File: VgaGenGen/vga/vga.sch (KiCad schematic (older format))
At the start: 26 parts, among them X25.175MHz CXO_DIP14

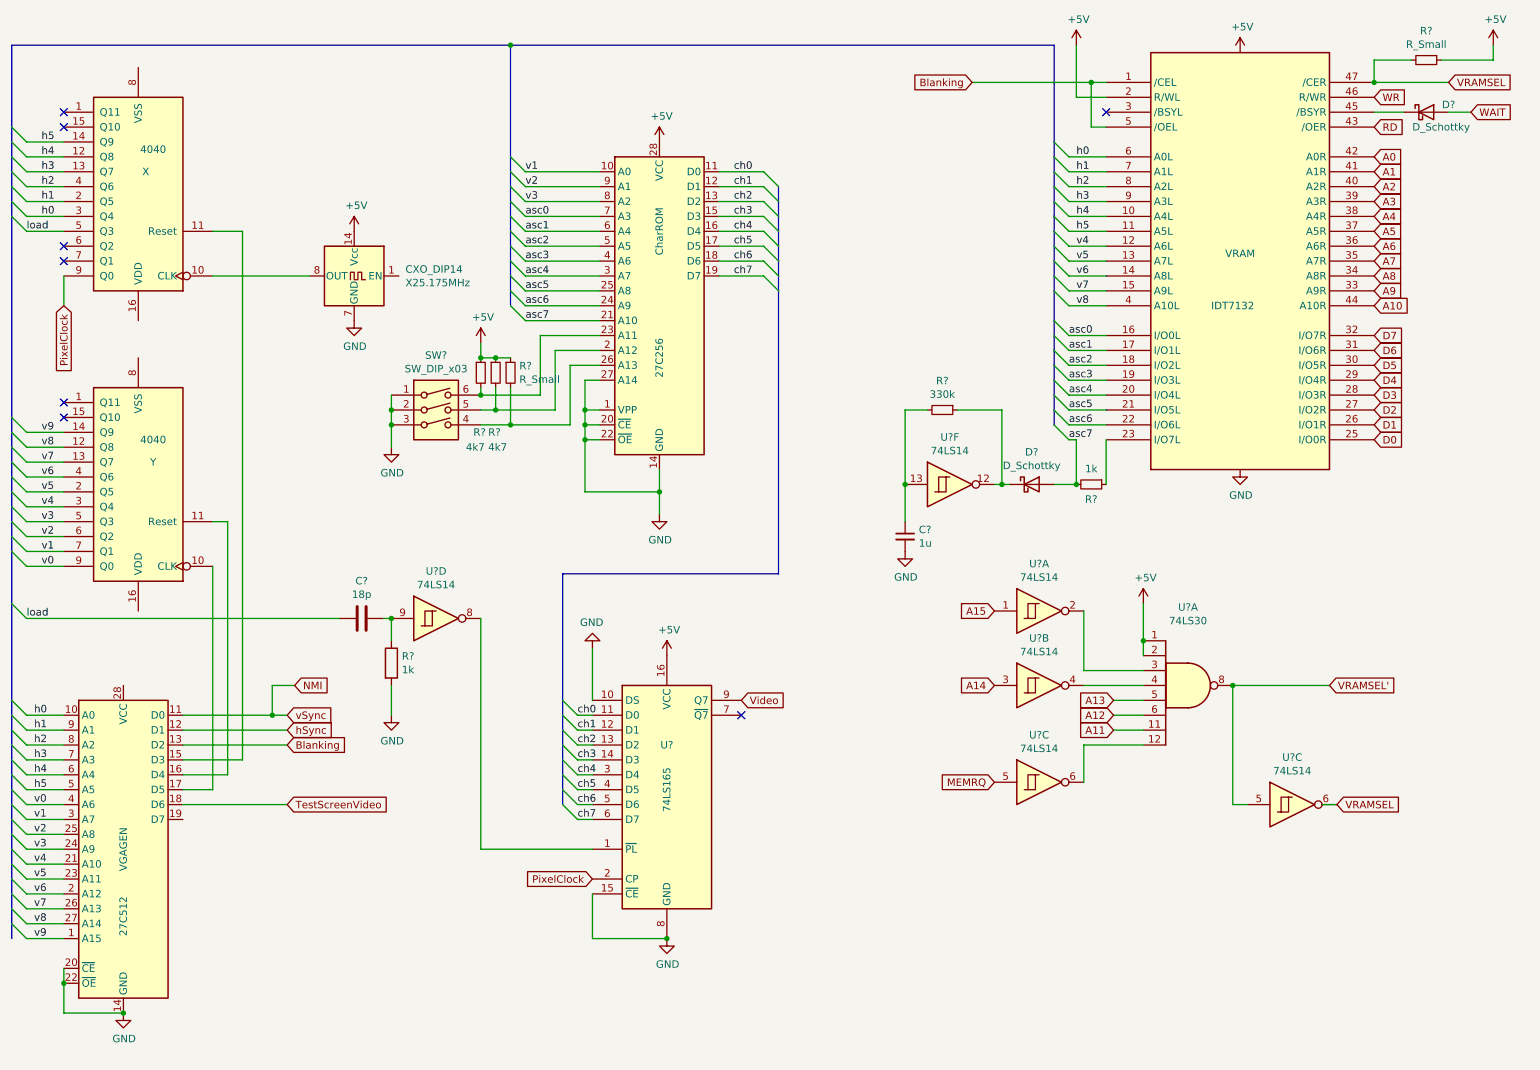
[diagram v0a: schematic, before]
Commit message: Compact Flash interface
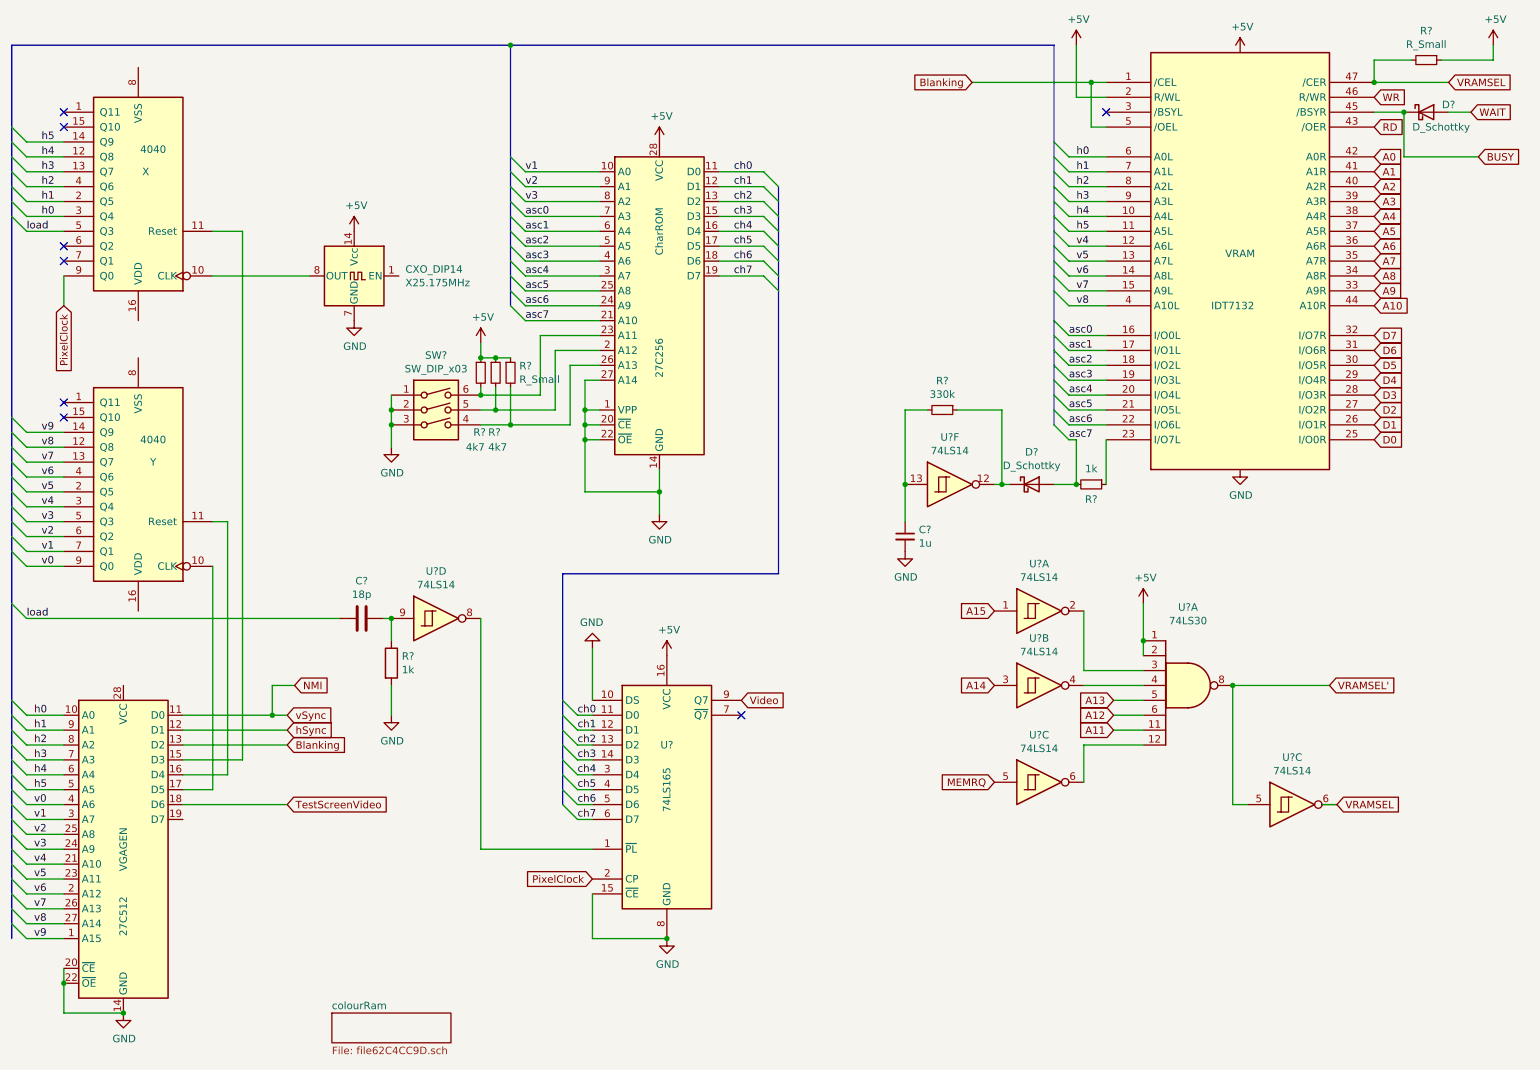
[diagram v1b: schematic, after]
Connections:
- net BUSY: now reaches D?.1 (K), VRAM.45 (/BSYR)
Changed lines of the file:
@@
 $Descr A4 11693 8268
 encoding utf-8
-Sheet 1 1
+Sheet 1 2
 Title ""
 Date ""
@@
 Wire Wire Line
 	6950 3900 6950 3650
+Connection ~ 6950 3650
+$Comp
+L power:GND #PWR?
+U 1 1 62829BE7
+P 6950 4100
+F 0 "#PWR?" H 6950 3850 50  0001 C CNN
+F 1 "GND" H 6955 3927 50  0000 C CNN
+F 2 "" H 6950 4100 50  0001 C CNN
+F 3 "" H 6950 4100 50  0001 C CNN
+	1    6950 4100
+	1    0    0    -1
+$EndComp
+$Sheet
+S 3100 7200 800  200
+U 62C4CC9E
+F0 "colourRam" 50
+F1 "file62C4CC9D.sch" 50
+$EndSheet
+Text GLabel 10800 1450 2    50   Input ~ 0
+BUSY
+Wire Wire Line
+	10800 1450 10300 1450
+Wire Wire Line
+	10300 1450 10300 1150
 Wire Bus Line
 	6100 1650 6100 4250
@@
 Wire Bus Line
 	950  700  950  6700
-Connection ~ 6950 3650
-$Comp
-L power:GND #PWR?
-U 1 1 62829BE7
-P 6950 4100
-F 0 "#PWR?" H 6950 3850 50  0001 C CNN
-F 1 "GND" H 6955 3927 50  0000 C CNN
-F 2 "" H 6950 4100 50  0001 C CNN
-F 3 "" H 6950 4100 50  0001 C CNN
-	1    6950 4100
-	1    0    0    -1
-$EndComp
+Connection ~ 10300 1150
 $EndSCHEMATC
